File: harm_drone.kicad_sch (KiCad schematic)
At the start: 19 parts, among them IC1 Microcontroller, J1 SYS_DEBUG

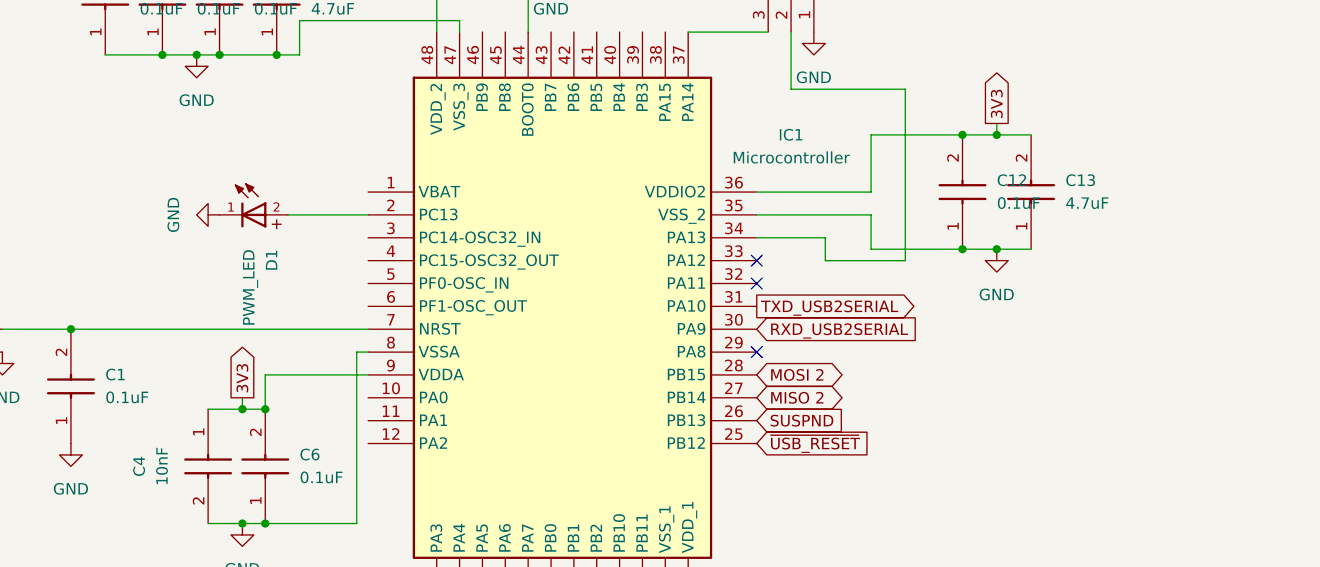
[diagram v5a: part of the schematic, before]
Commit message: USB fixes
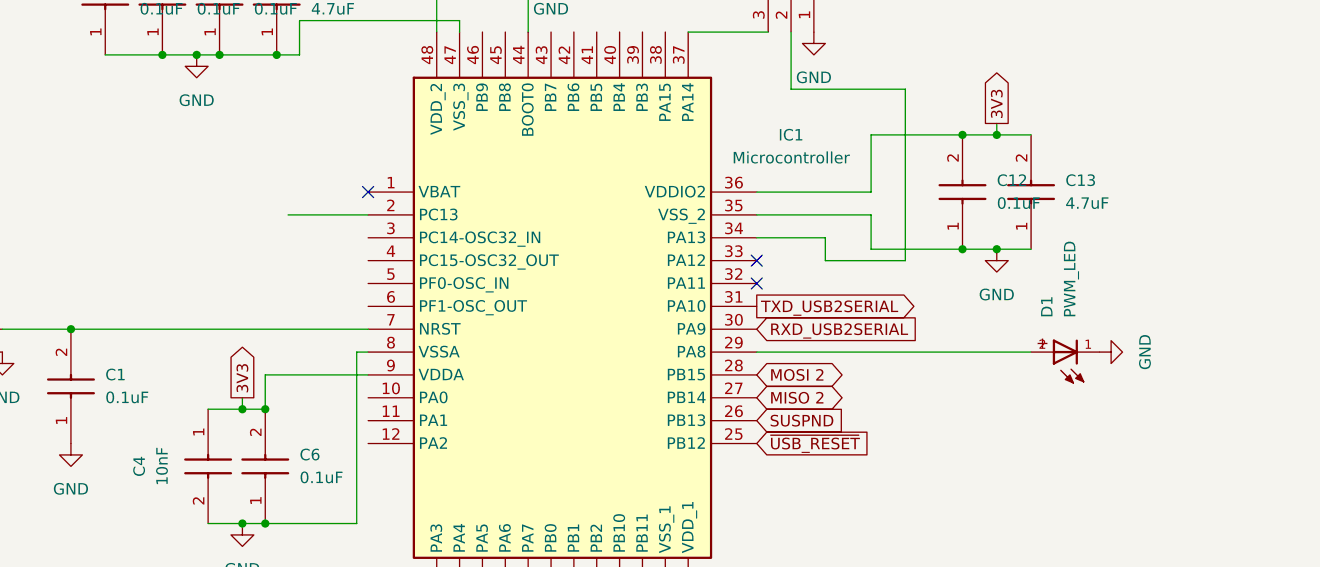
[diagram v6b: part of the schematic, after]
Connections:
- net at IC1.2 (PC13): no longer D1.2
- net at IC1.29 (PA8): now also D1.2
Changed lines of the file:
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@@
 	)
 	(no_connect
-		(at 161.29 115.57)
+		(at 118.11 97.79)
 	)
 	(no_connect
@@
 	(wire
 		(pts
+			(xy 161.29 115.57) (xy 191.77 115.57)
+		)
+		(stroke
+			(width 0)
+			(type default)
+		)
+	)
+	(wire
+		(pts
 			(xy 161.29 102.87) (xy 168.91 102.87)
 		)
@@
 	)
 	(symbol
-		(lib_id "power:GND")
-		(at 101.6 100.33 270)
-		(unit 1)
-		(exclude_from_sim no)
-		(in_bom yes)
-		(on_board yes)
-		(dnp no)
-		(fields_autoplaced yes)
-		(property "Reference" "#PWR04"
-			(at 95.25 100.33 0)
-			(effects
-				(font
-					(size 1.27 1.27)
-				)
-				(hide yes)
-			)
-		)
-		(property "Value" "GND"
-			(at 96.52 100.33 0)
-			(effects
-				(font
-					(size 1.27 1.27)
-				)
-			)
-		)
-		(property "Footprint" ""
-			(at 101.6 100.33 0)
-			(effects
-				(font
-					(size 1.27 1.27)
-				)
-				(hide yes)
-			)
-		)
-		(property "Datasheet" ""
-			(at 101.6 100.33 0)
-			(effects
-				(font
-					(size 1.27 1.27)
-				)
-				(hide yes)
-			)
-		)
-		(property "Description" "Power symbol creates a global label with name \"GND\" , ground"
-			(at 101.6 100.33 0)
-			(effects
-				(font
-					(size 1.27 1.27)
-				)
-				(hide yes)
-			)
-		)
-		(pin "1"
-		)
-		(instances
-			(project "harm_drone"
-				(path "/5ce3566e-4e0f-420e-9b0d-3952cd3c63fd"
-					(reference "#PWR04")
-					(unit 1)
-				)
-			)
-		)
-	)
-	(symbol
 		(lib_id "group127:0805Capacitor")
 		(at 95.25 82.55 90)
@@
 	)
 	(symbol
+		(lib_id "group127:PWM_LED")
+		(at 196.85 115.57 180)
+		(unit 1)
+		(exclude_from_sim no)
+		(in_bom yes)
+		(on_board yes)
+		(dnp no)
+		(fields_autoplaced yes)
+		(property "Reference" "D1"
+			(at 193.5616 111.76 90)
+			(effects
+				(font
+					(size 1.27 1.27)
+				)
+				(justify right)
+			)
+		)
+		(property "Value" "PWM_LED"
+			(at 196.1016 111.76 90)
+			(effects
+				(font
+					(size 1.27 1.27)
+				)
+				(justify right)
+			)
+		)
+		(property "Footprint" "group127:PWM_LED"
+			(at 196.85 115.57 0)
+			(effects
+				(font
+					(size 1.27 1.27)
+				)
+				(justify bottom)
+				(hide yes)
+			)
+		)
+		(property "Datasheet" ""
+			(at 196.85 115.57 0)
+			(effects
+				(font
+					(size 1.27 1.27)
+				)
+				(hide yes)
+			)
+		)
+		(property "Description" ""
+			(at 196.85 115.57 0)
+			(effects
+				(font
+					(size 1.27 1.27)
+				)
+				(hide yes)
+			)
+		)
+		(pin "1"
+		)
+		(pin "2"
+		)
+		(instances
+			(project "harm_drone"
+				(path "/5ce3566e-4e0f-420e-9b0d-3952cd3c63fd"
+					(reference "D1")
+					(unit 1)
+				)
+			)
+		)
+	)
+	(symbol
 		(lib_id "group127:0805Capacitor")
 		(at 100.33 121.92 90)
@@
 	)
 	(symbol
+		(lib_id "power:GND")
+		(at 199.39 115.57 90)
+		(unit 1)
+		(exclude_from_sim no)
+		(in_bom yes)
+		(on_board yes)
+		(dnp no)
+		(fields_autoplaced yes)
+		(property "Reference" "#PWR04"
+			(at 205.74 115.57 0)
+			(effects
+				(font
+					(size 1.27 1.27)
+				)
+				(hide yes)
+			)
+		)
+		(property "Value" "GND"
+			(at 204.47 115.57 0)
+			(effects
+				(font
+					(size 1.27 1.27)
+				)
+			)
+		)
+		(property "Footprint" ""
+			(at 199.39 115.57 0)
+			(effects
+				(font
+					(size 1.27 1.27)
+				)
+				(hide yes)
+			)
+		)
+		(property "Datasheet" ""
+			(at 199.39 115.57 0)
+			(effects
+				(font
+					(size 1.27 1.27)
+				)
+				(hide yes)
+			)
+		)
+		(property "Description" "Power symbol creates a global label with name \"GND\" , ground"
+			(at 199.39 115.57 0)
+			(effects
+				(font
+					(size 1.27 1.27)
+				)
+				(hide yes)
+			)
+		)
+		(pin "1"
+		)
+		(instances
+			(project "harm_drone"
+				(path "/5ce3566e-4e0f-420e-9b0d-3952cd3c63fd"
+					(reference "#PWR04")
+					(unit 1)
+				)
+			)
+		)
+	)
+	(symbol
 		(lib_id "group127:KSR221GLFS")
 		(at 77.47 115.57 180)
@@
 					(unit 1)
 				)
-			)
-		)
-	)
-	(symbol
-		(lib_id "group127:PWM_LED")
-		(at 104.14 100.33 0)
-		(unit 1)
-		(exclude_from_sim no)
-		(in_bom yes)
-		(on_board yes)
-		(dnp no)
-		(fields_autoplaced yes)
-		(property "Reference" "D1"
-			(at 107.4284 104.14 90)
-			(effects
-				(font
-					(size 1.27 1.27)
-				)
-				(justify right)
-			)
-		)
-		(property "Value" "PWM_LED"
-			(at 104.8884 104.14 90)
-			(effects
-				(font
-					(size 1.27 1.27)
-				)
-				(justify right)
-			)
-		)
-		(property "Footprint" "group127:PWM_LED"
-			(at 104.14 100.33 0)
-			(effects
-				(font
-					(size 1.27 1.27)
-				)
-				(justify bottom)
-				(hide yes)
-			)
-		)
-		(property "Datasheet" ""
-			(at 104.14 100.33 0)
-			(effects
-				(font
-					(size 1.27 1.27)
-				)
-				(hide yes)
-			)
-		)
-		(property "Description" ""
-			(at 104.14 100.33 0)
-			(effects
-				(font
-					(size 1.27 1.27)
-				)
-				(hide yes)
-			)
-		)
-		(pin "1"
-		)
-		(pin "2"
-		)
-		(instances
-			(project ""
-				(path "/5ce3566e-4e0f-420e-9b0d-3952cd3c63fd"
-					(reference "D1")
-					(unit 1)
-				)
